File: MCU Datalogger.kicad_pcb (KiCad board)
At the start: 2 copper layers, 51 x 29.9 mm, 32 parts, among them J1 Conn_01x04_Pin, J2 Conn_01x04_Pin, J3 Conn_01x09_Pin, J4 Conn_02x03_Odd_Even, U1 24LC1025, U2 24LC1025, U3 ATMEGA328P-AU, U4 DS1337S_, Y1 32.768kHz, Y2 16KHz

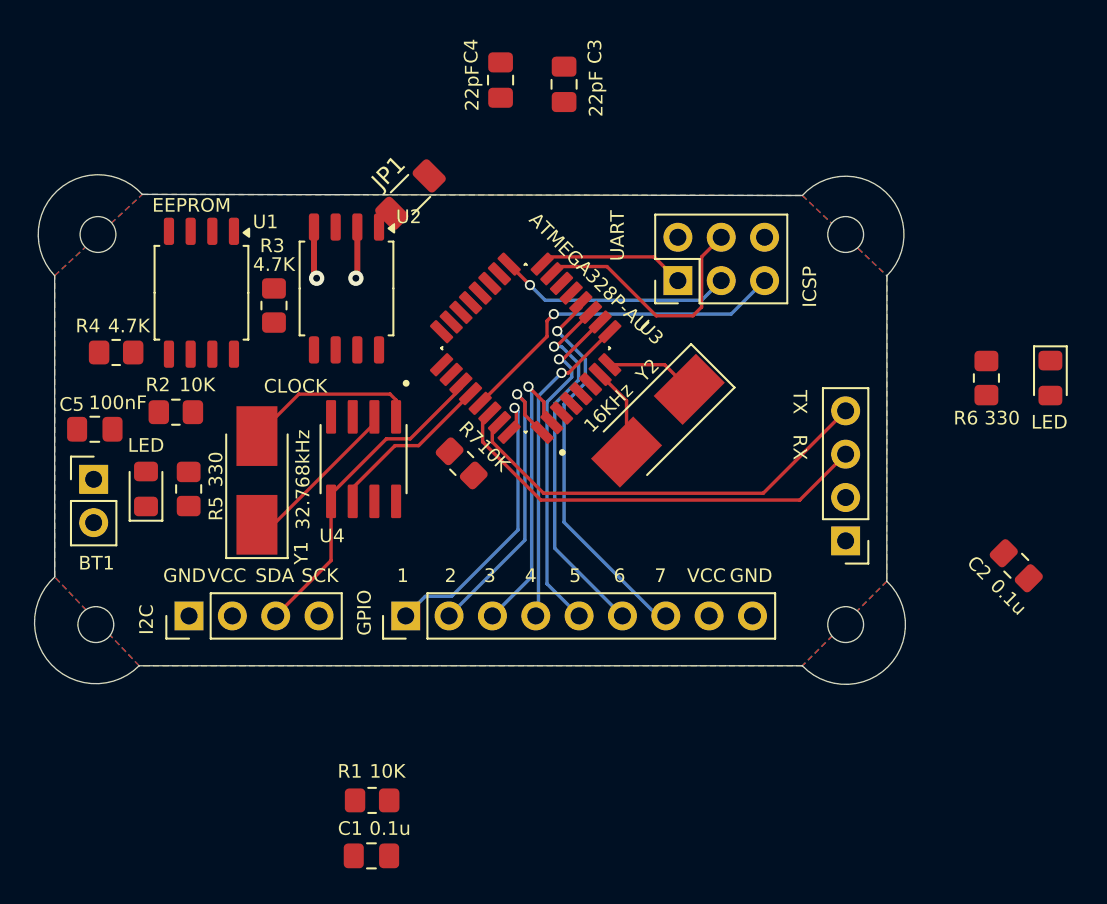
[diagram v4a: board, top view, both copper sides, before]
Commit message: finished an improved version of the 2 layer PCB
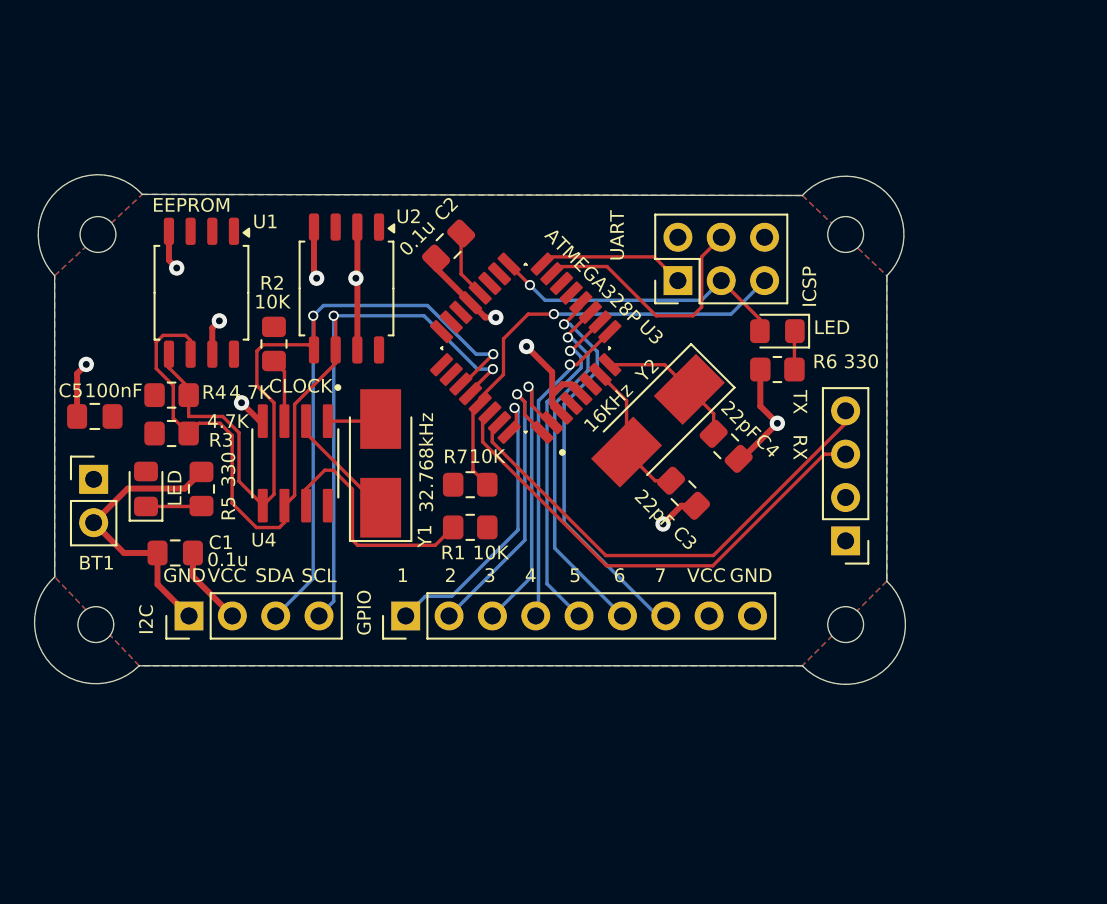
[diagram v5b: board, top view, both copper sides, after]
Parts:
- removed JP1: Jumper_2_Bridged, Resistor_SMD:R_1206_3216Metric_Pad1.30x1.75mm_HandSolder
- U3: value ATMEGA328P-AU -> ATMEGA328P
- moved C2 38.2 mm to (119.7, 93.5), turned to -135 degrees
- moved C4 25.2 mm to (136.0, 105.2), turned to -45 degrees
- moved C3 25.0 mm to (133.5, 108.0), turned to 135 degrees
- moved C1 21.1 mm to (103.7, 111.5), turned to 180 degrees
- moved R1 17.0 mm to (121.0, 110.0)
- moved D2 16.2 mm to (139.0, 98.5), turned to 180 degrees
- moved R6 12.3 mm to (139.0, 100.8), turned to 0 degrees
- moved R3 9.60 mm to (103.5, 104.5), turned to 0 degrees
- moved Y1 7.32 mm to (115.8, 106.2)
- moved R2 7.00 mm to (109.5, 99.2), turned to -90 degrees
- moved R4 4.10 mm to (103.5, 102.2)
- moved U4 4.01 mm to (110.8, 106.2)
- moved R7 1.35 mm to (121.0, 107.5), turned to 180 degrees
- moved C5 0.75 mm to (99.0, 103.5)
- moved R5 0.75 mm to (105.2, 107.8)
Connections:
- J1 pad 4: /SCK -> /SCL
- R3 pad 2: /SCK -> /SCL
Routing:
- net /SCL: track 9.98 -> 64.0 mm, vias 0 -> 2
- net GND: track 6.10 -> 58.0 mm, vias 2 -> 10
- net /SDA: track 18.9 -> 60.8 mm, vias 0 -> 2
- net Net-(U4-SQW/~INT): track 0.00 -> 14.1 mm
- net Net-(U4-X1): track 10.3 -> 3.15 mm
- net /RESET: track 20.2 -> 26.3 mm
- net /Vcc: track 0.00 -> 4.65 mm
- net Net-(U3-AREF): track 0.00 -> 3.95 mm
- net /SCK: track 13.8 -> 17.7 mm
- net Net-(U4-~{INTA}): track 0.00 -> 3.78 mm
- net /TX: track 25.3 -> 28.7 mm
- net Net-(U3-PB6): track 5.20 -> 8.50 mm
- net Net-(D1-K): track 0.00 -> 3.26 mm
- net Net-(U3-PB7): track 5.26 -> 8.45 mm
- net /RX: track 25.7 -> 28.9 mm
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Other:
- board text added: "SCL"
- board text removed: "SCK"
